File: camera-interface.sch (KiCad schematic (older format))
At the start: 44 parts, among them J8 WE_68715014522, U19 NTS0102GT, U20 NTS0102GT, U22 AP2114H-3_3TRG1

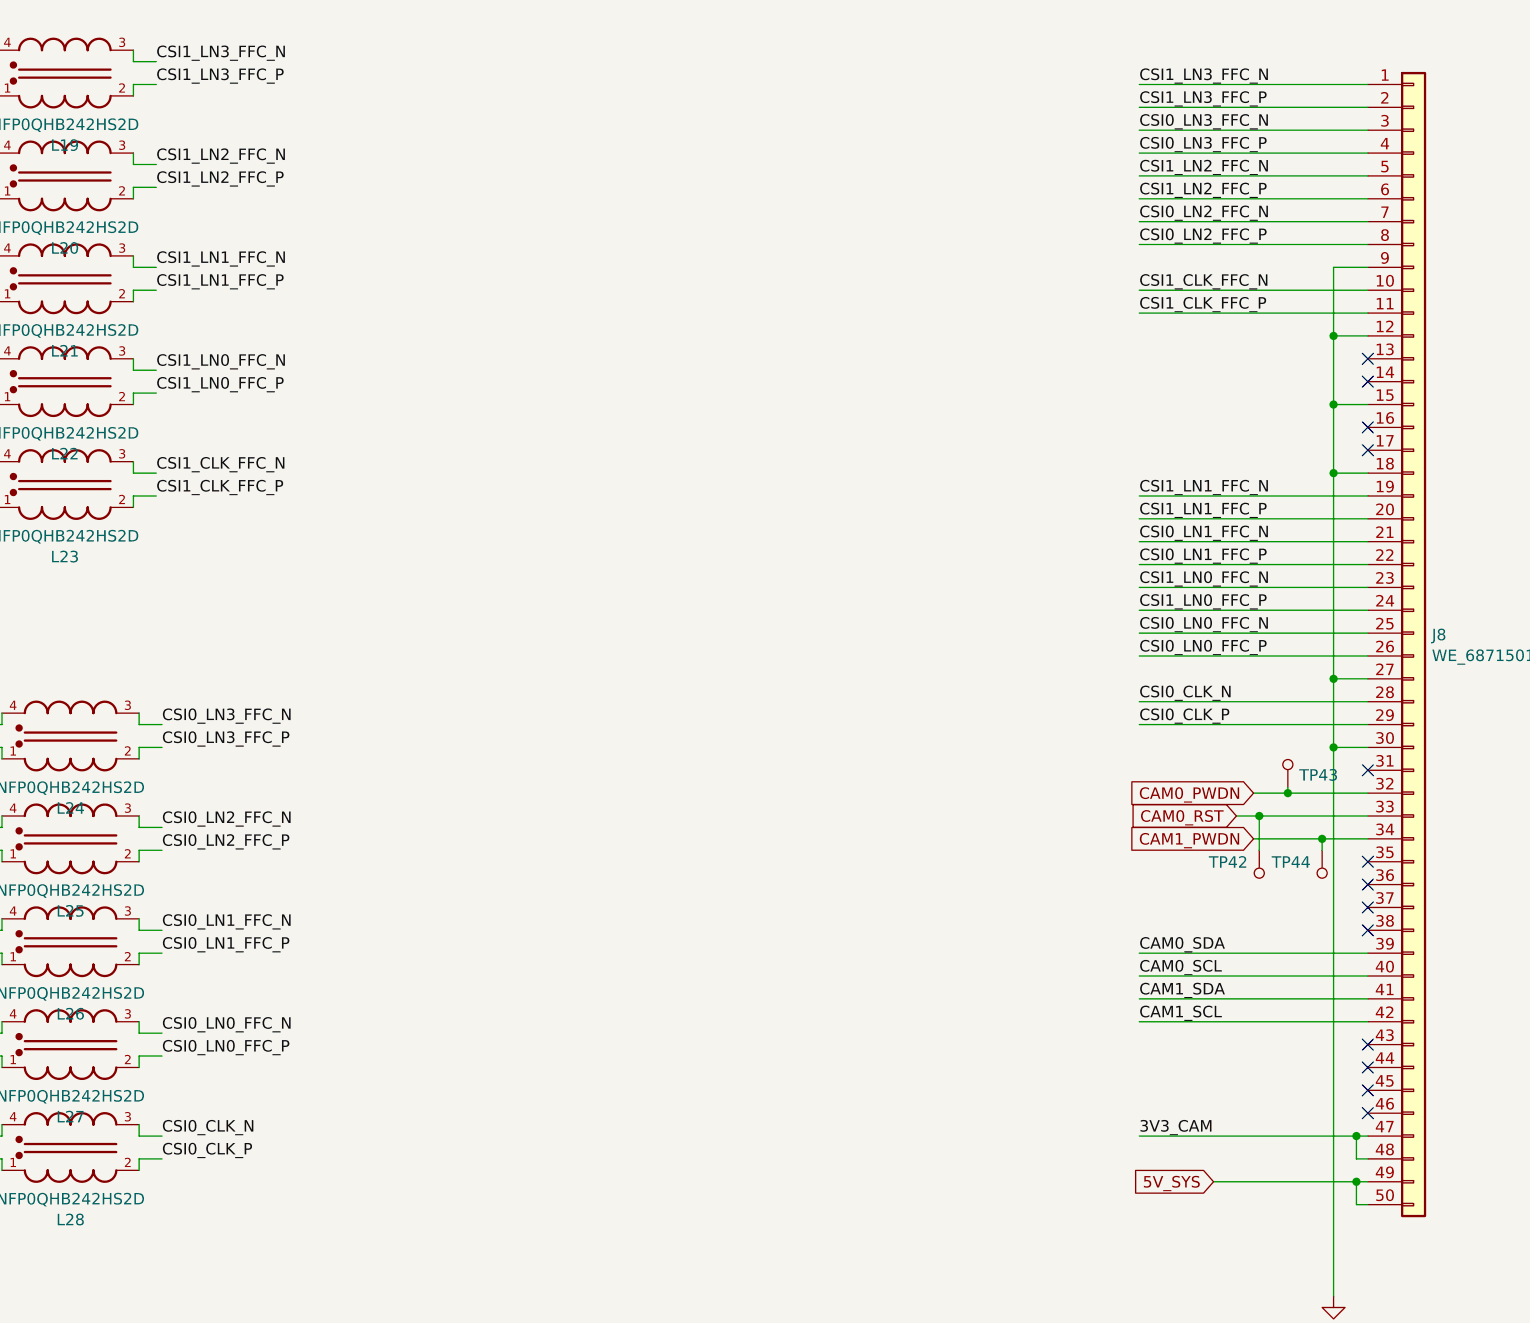
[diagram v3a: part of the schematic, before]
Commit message: Fix mixed up lanes
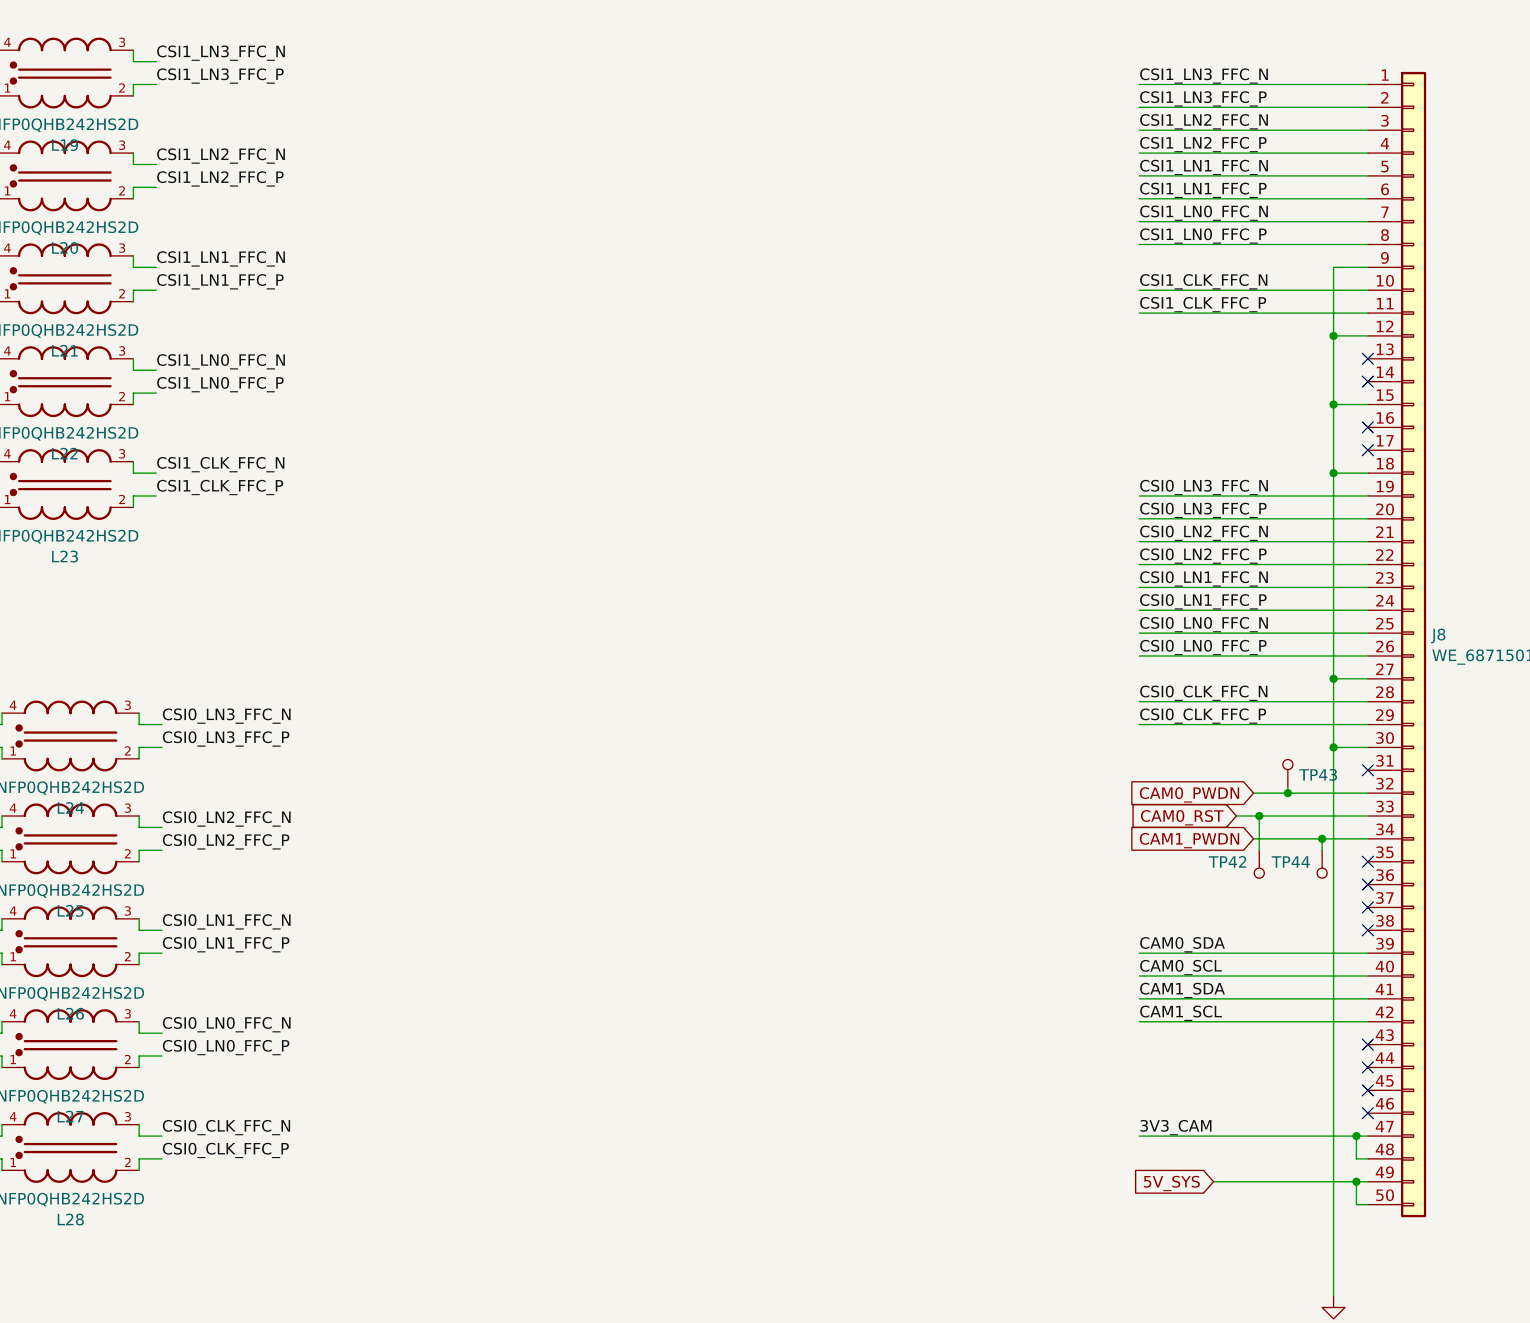
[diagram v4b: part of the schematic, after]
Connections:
- net CSI0_CLK_N: no longer J8.28 (Pin_28), L28.3
- net CSI0_CLK_P: no longer J8.29 (Pin_29), L28.2
- net CSI0_LN1_FFC_N: now also J8.23 (Pin_23); no longer J8.21 (Pin_21)
- net CSI0_LN1_FFC_P: now also J8.24 (Pin_24); no longer J8.22 (Pin_22)
- net CSI0_LN2_FFC_N: now also J8.21 (Pin_21); no longer J8.7 (Pin_7)
- net CSI0_LN2_FFC_P: now also J8.22 (Pin_22); no longer J8.8 (Pin_8)
- net CSI0_LN3_FFC_N: now also J8.19 (Pin_19); no longer J8.3 (Pin_3)
- net CSI0_LN3_FFC_P: now also J8.20 (Pin_20); no longer J8.4 (Pin_4)
- net CSI1_LN0_FFC_N: now also J8.7 (Pin_7); no longer J8.23 (Pin_23)
- net CSI1_LN0_FFC_P: now also J8.8 (Pin_8); no longer J8.24 (Pin_24)
- net CSI1_LN1_FFC_N: now also J8.5 (Pin_5); no longer J8.19 (Pin_19)
- net CSI1_LN1_FFC_P: now also J8.6 (Pin_6); no longer J8.20 (Pin_20)
- net CSI1_LN2_FFC_N: now also J8.3 (Pin_3); no longer J8.5 (Pin_5)
- net CSI1_LN2_FFC_P: now also J8.4 (Pin_4); no longer J8.6 (Pin_6)
- new net CSI0_CLK_FFC_N: J8.28 (Pin_28), L28.3
- new net CSI0_CLK_FFC_P: J8.29 (Pin_29), L28.2
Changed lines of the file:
@@
 Text Label 2175 4550 0    50   ~ 0
 CSI0_LN3_FFC_P
-Text Label 6450 1850 0    50   ~ 0
+Text Label 6450 3450 0    50   ~ 0
 CSI0_LN3_FFC_N
-Text Label 6450 1950 0    50   ~ 0
+Text Label 6450 3550 0    50   ~ 0
 CSI0_LN3_FFC_P
 Wire Wire Line
@@
 CSI0_LN0_FFC_P
 Text Label 2175 6250 0    50   ~ 0
-CSI0_CLK_N
+CSI0_CLK_FFC_N
 Text Label 2175 6350 0    50   ~ 0
-CSI0_CLK_P
-Text Label 6450 2050 0    50   ~ 0
+CSI0_CLK_FFC_P
+Text Label 6450 1850 0    50   ~ 0
 CSI1_LN2_FFC_N
-Text Label 6450 2150 0    50   ~ 0
+Text Label 6450 1950 0    50   ~ 0
 CSI1_LN2_FFC_P
-Text Label 6450 2250 0    50   ~ 0
+Text Label 6450 3650 0    50   ~ 0
 CSI0_LN2_FFC_N
-Text Label 6450 2350 0    50   ~ 0
+Text Label 6450 3750 0    50   ~ 0
 CSI0_LN2_FFC_P
 Wire Wire Line
@@
 	6450 1750 7450 1750
 Wire Wire Line
+	6450 3450 7450 3450
+Wire Wire Line
+	6450 3550 7450 3550
+Wire Wire Line
 	6450 1850 7450 1850
 Wire Wire Line
 	6450 1950 7450 1950
 Wire Wire Line
-	6450 2050 7450 2050
-Wire Wire Line
-	6450 2150 7450 2150
-Wire Wire Line
-	6450 2250 7450 2250
-Wire Wire Line
-	6450 2350 7450 2350
+	6450 3650 7450 3650
+Wire Wire Line
+	6450 3750 7450 3750
 Text Label 6450 2550 0    50   ~ 0
 CSI1_CLK_FFC_N
@@
 	7300 3350 7300 4250
 Wire Wire Line
-	7450 3450 6450 3450
-Wire Wire Line
-	7450 3550 6450 3550
-Text Label 6450 3450 0    50   ~ 0
+	7450 2050 6450 2050
+Wire Wire Line
+	7450 2150 6450 2150
+Text Label 6450 2050 0    50   ~ 0
 CSI1_LN1_FFC_N
-Text Label 6450 3550 0    50   ~ 0
+Text Label 6450 2150 0    50   ~ 0
 CSI1_LN1_FFC_P
-Text Label 6450 3650 0    50   ~ 0
-CSI0_LN1_FFC_N
-Text Label 6450 3750 0    50   ~ 0
-CSI0_LN1_FFC_P
-Wire Wire Line
-	6450 3650 7450 3650
-Wire Wire Line
-	6450 3750 7450 3750
-Text Label 6450 3850 0    50   ~ 0
-CSI1_LN0_FFC_N
-Text Label 6450 3950 0    50   ~ 0
-CSI1_LN0_FFC_P
 Text Label 6450 4050 0    50   ~ 0
 CSI0_LN0_FFC_N
@@
 	6450 4050 7450 4050
 Wire Wire Line
-	6450 3950 7450 3950
-Wire Wire Line
-	6450 3850 7450 3850
-Wire Wire Line
 	7450 4250 7300 4250
 Connection ~ 7300 4250
 Wire Wire Line
 	7300 4250 7300 4550
-Text Label 6450 4350 0    50   ~ 0
-CSI0_CLK_N
-Text Label 6450 4450 0    50   ~ 0
-CSI0_CLK_P
 Wire Wire Line
 	6450 4450 7450 4450
@@
 Wire Wire Line
 	7250 4950 6950 4950
+Wire Wire Line
+	6450 3950 7450 3950
+Wire Wire Line
+	6450 3850 7450 3850
+Text Label 6450 3950 0    50   ~ 0
+CSI0_LN1_FFC_P
+Text Label 6450 3850 0    50   ~ 0
+CSI0_LN1_FFC_N
+Wire Wire Line
+	6450 2250 7450 2250
+Wire Wire Line
+	6450 2350 7450 2350
+Text Label 6450 2350 0    50   ~ 0
+CSI1_LN0_FFC_P
+Text Label 6450 2250 0    50   ~ 0
+CSI1_LN0_FFC_N
+Text Label 6450 4350 0    50   ~ 0
+CSI0_CLK_FFC_N
+Text Label 6450 4450 0    50   ~ 0
+CSI0_CLK_FFC_P
 $EndSCHEMATC

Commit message: Fix labels
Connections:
- net CAM0_SCL is gone; now on net CCI0_I2C_SCL_3V3: J8.40 (Pin_40)
- net CAM0_SDA is gone; now on net CCI0_I2C_SDA_3V3: J8.39 (Pin_39)
- net CAM1_SCL is gone; now on net CCI1_I2C_SCL_3V3: J8.42 (Pin_42)
- net CAM1_SDA is gone; now on net CCI1_I2C_SDA_3V3: J8.41 (Pin_41)
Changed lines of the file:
@@
 NoConn ~ 7450 5250
 NoConn ~ 7450 5350
-Text Label 6450 5450 0    50   ~ 0
-CAM0_SDA
-Text Label 6450 5550 0    50   ~ 0
-CAM0_SCL
-Text Label 6450 5650 0    50   ~ 0
-CAM1_SDA
-Text Label 6450 5750 0    50   ~ 0
-CAM1_SCL
-Wire Wire Line
-	6450 5450 7450 5450
-Wire Wire Line
-	6450 5550 7450 5550
 Wire Wire Line
 	6450 5650 7450 5650
@@
 Text Label 6450 4450 0    50   ~ 0
 CSI0_CLK_FFC_P
+Wire Wire Line
+	6450 5450 7450 5450
+Wire Wire Line
+	6450 5550 7450 5550
+Text Label 6450 5450 0    50   ~ 0
+CCI0_I2C_SDA_3V3
+Text Label 6450 5550 0    50   ~ 0
+CCI0_I2C_SCL_3V3
+Text Label 6450 5650 0    50   ~ 0
+CCI1_I2C_SDA_3V3
+Text Label 6450 5750 0    50   ~ 0
+CCI1_I2C_SCL_3V3
 $EndSCHEMATC

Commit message: Cleanup
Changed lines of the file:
@@
 $Descr A3 16535 11693
 encoding utf-8
-Sheet 7 13
+Sheet 7 12
 Title ""
 Date ""
@@
 $EndComp
 Wire Wire Line
-	2050 1550 2150 1550
-Wire Wire Line
-	2050 1650 2150 1650
-Text Label 2150 1550 0    50   ~ 0
+	2050 1550 2750 1550
+Wire Wire Line
+	2050 1650 2750 1650
+Text Label 2750 1550 2    50   ~ 0
 CSI1_LN3_FFC_N
-Text Label 2150 1650 0    50   ~ 0
+Text Label 2750 1650 2    50   ~ 0
 CSI1_LN3_FFC_P
 Text Label 6450 1650 0    50   ~ 0
@@
 Text Label 6450 1750 0    50   ~ 0
 CSI1_LN3_FFC_P
-Text Label 2175 4450 0    50   ~ 0
+Text Label 2750 4450 2    50   ~ 0
 CSI0_LN3_FFC_N
-Text Label 2175 4550 0    50   ~ 0
+Text Label 2750 4550 2    50   ~ 0
 CSI0_LN3_FFC_P
 Text Label 6450 3450 0    50   ~ 0
@@
 CSI0_LN3_FFC_P
 Wire Wire Line
-	2075 4450 2175 4450
-Wire Wire Line
-	2075 4550 2175 4550
+	2075 4450 2750 4450
+Wire Wire Line
+	2075 4550 2750 4550
 Wire Wire Line
 	2050 1950 2050 2000
 Wire Wire Line
-	2050 2000 2150 2000
+	2050 2000 2750 2000
 Wire Wire Line
 	2050 2150 2050 2100
 Wire Wire Line
-	2050 2100 2150 2100
+	2050 2100 2750 2100
 Wire Wire Line
 	2050 2400 2050 2450
 Wire Wire Line
-	2050 2450 2150 2450
+	2050 2450 2750 2450
 Wire Wire Line
 	2050 2600 2050 2550
 Wire Wire Line
-	2050 2550 2150 2550
+	2050 2550 2750 2550
 Wire Wire Line
 	2050 2850 2050 2900
 Wire Wire Line
-	2050 2900 2150 2900
+	2050 2900 2750 2900
 Wire Wire Line
 	2050 3050 2050 3000
 Wire Wire Line
-	2050 3000 2150 3000
+	2050 3000 2750 3000
 Wire Wire Line
 	2050 3300 2050 3350
 Wire Wire Line
-	2050 3350 2150 3350
+	2050 3350 2750 3350
 Wire Wire Line
 	2050 3500 2050 3450
 Wire Wire Line
-	2050 3450 2150 3450
-Text Label 2150 2000 0    50   ~ 0
+	2050 3450 2750 3450
+Text Label 2750 2000 2    50   ~ 0
 CSI1_LN2_FFC_N
-Text Label 2150 2100 0    50   ~ 0
+Text Label 2750 2100 2    50   ~ 0
 CSI1_LN2_FFC_P
-Text Label 2150 2550 0    50   ~ 0
+Text Label 2750 2550 2    50   ~ 0
 CSI1_LN1_FFC_P
-Text Label 2150 2450 0    50   ~ 0
+Text Label 2750 2450 2    50   ~ 0
 CSI1_LN1_FFC_N
-Text Label 2150 2900 0    50   ~ 0
+Text Label 2750 2900 2    50   ~ 0
 CSI1_LN0_FFC_N
-Text Label 2150 3000 0    50   ~ 0
+Text Label 2750 3000 2    50   ~ 0
 CSI1_LN0_FFC_P
-Text Label 2150 3350 0    50   ~ 0
+Text Label 2750 3350 2    50   ~ 0
 CSI1_CLK_FFC_N
-Text Label 2150 3450 0    50   ~ 0
+Text Label 2750 3450 2    50   ~ 0
 CSI1_CLK_FFC_P
 Wire Wire Line
 	2075 4850 2075 4900
 Wire Wire Line
-	2075 4900 2175 4900
+	2075 4900 2750 4900
 Wire Wire Line
 	2075 5050 2075 5000
 Wire Wire Line
-	2075 5000 2175 5000
+	2075 5000 2750 5000
 Wire Wire Line
 	2075 5300 2075 5350
 Wire Wire Line
-	2075 5350 2175 5350
+	2075 5350 2750 5350
 Wire Wire Line
 	2075 5500 2075 5450
 Wire Wire Line
-	2075 5450 2175 5450
+	2075 5450 2750 5450
 Wire Wire Line
 	2075 5750 2075 5800
 Wire Wire Line
-	2075 5800 2175 5800
+	2075 5800 2750 5800
 Wire Wire Line
 	2075 5950 2075 5900
 Wire Wire Line
-	2075 5900 2175 5900
+	2075 5900 2750 5900
 Wire Wire Line
 	2075 6200 2075 6250
 Wire Wire Line
-	2075 6250 2175 6250
+	2075 6250 2750 6250
 Wire Wire Line
 	2075 6400 2075 6350
 Wire Wire Line
-	2075 6350 2175 6350
-Text Label 2175 4900 0    50   ~ 0
+	2075 6350 2750 6350
+Text Label 2750 4900 2    50   ~ 0
 CSI0_LN2_FFC_N
-Text Label 2175 5000 0    50   ~ 0
+Text Label 2750 5000 2    50   ~ 0
 CSI0_LN2_FFC_P
-Text Label 2175 5350 0    50   ~ 0
+Text Label 2750 5350 2    50   ~ 0
 CSI0_LN1_FFC_N
-Text Label 2175 5450 0    50   ~ 0
+Text Label 2750 5450 2    50   ~ 0
 CSI0_LN1_FFC_P
-Text Label 2175 5800 0    50   ~ 0
+Text Label 2750 5800 2    50   ~ 0
 CSI0_LN0_FFC_N
-Text Label 2175 5900 0    50   ~ 0
+Text Label 2750 5900 2    50   ~ 0
 CSI0_LN0_FFC_P
-Text Label 2175 6250 0    50   ~ 0
+Text Label 2750 6250 2    50   ~ 0
 CSI0_CLK_FFC_N
-Text Label 2175 6350 0    50   ~ 0
+Text Label 2750 6350 2    50   ~ 0
 CSI0_CLK_FFC_P
 Text Label 6450 1850 0    50   ~ 0
